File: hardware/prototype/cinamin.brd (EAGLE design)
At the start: 160 x 100 mm, 93 parts, among them J1 TC2030-JLINK-L, Q1 MOSFET-NCHANNELXFDN-3, Q2 MOSFET-NCHANNELXFDN-3, Q5 MOSFET-NCHANNELXFDN-3, U1 ADM8641, U11 ADM8641, U2 ADM8641, U3 BQ25504RGT

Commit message: most of the way through layout
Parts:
- removed JP21: TO_BQ25504, SparkFun-Passives:1X02
- removed JP23: FOR_BQ25504, SparkFun-Passives:1X02
- removed U$10, U$5: U1, chips:DFN-8
- removed U$11: M08X2, SparkFun-Connectors:2X8
- removed U$12: (no value), chips:TSOP-10
- removed U$13: (no value), fets:XFDFN-3
- removed U$6: (no value), chips:QFN-48-6MM
- removed U11: ADM8641, chips:WLCSP-6
- added PV_TO_CAPS: FOR_BQ25504, SparkFun-Passives:1X02
- added Q13: (no value), fets:XFDFN-3
- added R16: 2.2k, passives:0402_RES
- added RESET: B3U-1000P, switches:B3U-1000P
- added SOLAR_TO_BQ: TO_BQ25504, SparkFun-Passives:1X02
- added SUPPLY_SELECTOR: M08X2, SparkFun-Connectors:2X8
- added TP3, TP4, TP5, TP6, TP7, TP8: TPSPAD1-13, testpad:P1-13
- added U4, U5: U1, chips:DFN-8
- added U6: ADM8641, chips:WLCSP-6
- added U7: (no value), chips:TSOP-10
- added U9: (no value), chips:QFN-48-6MM
- JP22: value (none) -> TO_BLE
- JP24: value (none) -> TO_BQ25504
- TP1, TP2: value TPSQB1,27 -> TPSPAD1-13; device testpad:B1,27 -> testpad:P1-13
- moved JP24 453.2 mm to (20.0, 11.8), flipped to the bottom, turned to 180 degrees
- moved JP22 449.9 mm to (27.4, 11.8)
- moved C14 440.8 mm to (22.8, 9.30), turned to 180 degrees
- moved R22 432.9 mm to (19.1, 5.70), turned to 90 degrees
- moved R21 427.5 mm to (19.1, 3.90), turned to 90 degrees
- moved R20 426.1 mm to (21.0, 5.70), turned to 90 degrees
- moved R19 420.7 mm to (21.0, 3.90), turned to 90 degrees
- moved C13 417.2 mm to (27.8, 6.20), turned to 270 degrees
- moved R18 416.9 mm to (22.3, 3.50), turned to 180 degrees
- moved C12 414.2 mm to (26.8, 6.20), turned to 270 degrees
- moved C11 401.9 mm to (19.9, 8.20), turned to 270 degrees
- moved L3 399.3 mm to (21.2, 8.00), turned to 90 degrees
- moved JP20 391.2 mm to (42.6, 23.8)
- moved JP18 389.2 mm to (38.2, 37.5)
- moved JP19 382.2 mm to (35.4, 23.7)
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- renumbered U$8 to U8
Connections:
- removed net N$48: C14.2, R18.1, R21.1
- new net HIGH: JP20.1, Q10.D
- new net N$52: J1.2, U9.30
- new net N$53: J1.4, U9.31
- new net N$56: R16.2, RESET.1, U9.21
- new net OUT: JP2.1, R3.1, U4.P8
- new net OUT2: JP22.1, Q13.D
- new net VDD: JP19.2, Q10.S, U7.10
- new net VIN_DC: JP24.2, U3.2
- new net VSTOR: C12.1, C13.1, Q13.S, U3.15, U3.3
- net 580_VBAT: now also J1.1, RESET.2, U9.17, U9.19; no longer C12.1, C13.1, JP2.1, JP20.1, JP22.1, Q10.D, R3.1, U$13.D, U$13.S, U$5.P8, U$6.17, U$6.19, U3.15, U3.3
- net ADM8641: now also SUPPLY_SELECTOR.6; no longer U$11.6
- net ADM8641_2: now also SUPPLY_SELECTOR.12; no longer U$11.12
- net AP4400: now also SUPPLY_SELECTOR.10; no longer JP19.2, Q10.S, U$11.10, U$12.10
- net BQ25504: now also SUPPLY_SELECTOR.8; no longer U$11.8
- net GND: now also C14.2, J1.5, R16.1, R18.1, R21.1, TP6.TP, TP7.TP, TP8.TP, U4.P$1, U4.P1, U4.P2, U5.P$1, U5.P1, U5.P2, U6.A2, U6.B2, U7.5, U9.20, U9.28, U9.41, U9.GND; no longer U$10.P$1, U$10.P1, U$10.P2, U$12.5, U$5.P$1, U$5.P1, U$5.P2, U$6.20, U$6.28, U$6.41, U$6.GND, U11.A2, U11.B2
- net LTC1540_E_HYST: now also SUPPLY_SELECTOR.4; no longer U$11.4
- net LTC1540_I_HYST: now also SUPPLY_SELECTOR.2; no longer U$11.2
- net N$1: now also PV_TO_CAPS.2, SUPPLY_SELECTOR.1, SUPPLY_SELECTOR.11, SUPPLY_SELECTOR.3, SUPPLY_SELECTOR.5, SUPPLY_SELECTOR.7, SUPPLY_SELECTOR.9; no longer JP23.2, U$11.1, U$11.11, U$11.3, U$11.5, U$11.7, U$11.9
- net N$10: now also U9.34; no longer U$6.34
- net N$11: now also U9.35; no longer U$6.35
- net N$14: now also U5.P3; no longer U$10.P3
- net N$2: now also U5.P4, U5.P5, U5.P6; no longer U$10.P4, U$10.P5, U$10.P6
- net N$20: now also U5.P7; no longer U$10.P7
- net N$28: now also U4.P7; no longer U$5.P7
- net N$29: now also U6.C2; no longer U11.C2
- net N$3: now also U4.P3; no longer U$5.P3
- net N$35: now also U6.A1; no longer U11.A1
- net N$37: now also U7.6; no longer U$12.6
- net N$4: now also U4.P4, U4.P5, U4.P6; no longer U$5.P4, U$5.P5, U$5.P6
- net N$43: now also PV_TO_CAPS.1, SOLAR_TO_BQ.1, TP3.TP, TP4.TP, TP5.TP; no longer JP21.1, JP23.1
- net N$47: now also Q13.G; no longer U$13.G
- net N$5: now also U9.42; no longer U$6.42
- net N$7: now also U9.26; no longer U$6.26
- net N$8: now also U9.23, U9.37; no longer U$6.23, U$6.37
- net N$9: now also U5.P8; no longer U$10.P8
- net PV: now also SOLAR_TO_BQ.2; no longer JP21.2, JP24.2, U3.2
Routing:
- net N$43: track 0.00 -> 53.8 mm
- net N$1: track 0.00 -> 32.1 mm
- net 580_VBAT: track 0.00 -> 31.3 mm
- net N$52: track 0.00 -> 16.1 mm
- net N$8: track 0.00 -> 15.6 mm, vias 0 -> 2
- net GND: track 0.00 -> 15.0 mm, vias 0 -> 39
- net PV: track 0.00 -> 14.7 mm
- net ADM8641: track 0.00 -> 14.4 mm
- net VSTOR: track 0.00 -> 14.0 mm
- net N$19: track 0.00 -> 13.1 mm
- net N$41: track 0.00 -> 12.0 mm, vias 0 -> 2
- net N$53: track 0.00 -> 11.2 mm
- net LTC1540_E_HYST: track 0.00 -> 11.1 mm
- net N$47: track 0.00 -> 9.80 mm
- net N$25: track 0.00 -> 9.63 mm
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- added copper zone on layer 1, net GND
- added copper zone on layer 16, net GND
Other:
- board text added: "ADM8641_1"
- board text added: "ADM8641_2"
- board text added: "AP4400"
- board text added: "BQ25504"
- board text added: "Bluetooth"
- board text added: "Buffer Caps"
- board text added: "LTC1540_1"
- board text added: "LTC1540_2"
- board text added: "PV+"
- board text added: "PV-"
- board text removed: "Example BLE Layout"

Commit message: layout and schematic done
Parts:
- removed JP1, JP12, JP2, JP3: TO_BLE, SparkFun-Passives:1X02
- removed JP10, JP5: INPUT_DIVIDER, SparkFun-Passives:1X02
- removed JP11: TO_LTC1540, SparkFun-Passives:1X02
- removed JP13, JP6: STAGE_1_PULL, SparkFun-Passives:1X02
- removed JP14, JP7: STAGE_2_PULL, SparkFun-Passives:1X02
- removed JP15, JP9: OFF_DIVIDER, SparkFun-Passives:1X02
- removed JP16: TO_ADM, SparkFun-Passives:1X02
- removed JP17: TO_ADM2, SparkFun-Passives:1X02
- removed JP18: TO_ADM1, SparkFun-Passives:1X02
- removed JP19, JP20: TO_AP440, SparkFun-Passives:1X02
- removed JP4: (no value), SparkFun-Passives:1X02
- removed JP8: TO_LATCH, SparkFun-Passives:1X02
- removed U$7: AF212M, chips:AH212M
- added A1: (no value), chips:AH212M
- added J10, J15, J18, J3: TO_BLE, SparkFun-Passives:1X02
- added J11: TO_ADM, SparkFun-Passives:1X02
- added J12, J7: STAGE_1_PULL, SparkFun-Passives:1X02
- added J13, J8: STAGE_2_PULL, SparkFun-Passives:1X02
- added J14, J9: OFF_DIVIDER, SparkFun-Passives:1X02
- added J16: TO_ADM2, SparkFun-Passives:1X02
- added J17: TO_ADM1, SparkFun-Passives:1X02
- added J19, J20: TO_AP440, SparkFun-Passives:1X02
- added J2: TO_LTC1540, SparkFun-Passives:1X02
- added J4: INPUT_DIVIDER, SparkFun-Passives:1X02
- added J5: (no value), SparkFun-Passives:1X02
- added J6: TO_LATCH, SparkFun-Passives:1X02
- added PROG: TC2030-JLINK-L, connector:TC2030-IDC
- J1: value TC2030-JLINK-L -> INPUT_DIVIDER; device connector:TC2030-IDC -> SparkFun-Passives:1X02
- R1, R4: value (none) -> 2.2M
- R10, R11, R12, R13, R14, R15, R6, R7, R8, R9: value (none) -> 1M
- R2, R5: value (none) -> 1.18M
- R3: value (none) -> 3M
- U$9: device chips:AH212M -> chips:AH212M@1
- U1: value ADM8641 -> 3.048
- U2: value ADM8641 -> 2.3
- moved X1 92.4 mm to (68.6, 5.61), turned to 90 degrees
- moved C7 92.3 mm to (73.4, 4.46), turned to 180 degrees
- moved U9 84.0 mm to (74.0, 8.50), turned to 180 degrees
- moved L1 83.1 mm to (69.4, 10.3), turned to 180 degrees
- moved C5 80.3 mm to (69.0, 12.1), turned to 90 degrees
- moved C2 79.8 mm to (69.8, 12.1), turned to 90 degrees
- moved J1 79.0 mm to (49.8, 36.6)
- moved R16 74.3 mm to (72.9, 13.8), turned to 180 degrees
- moved RESET 70.8 mm to (72.9, 15.6), turned to 0 degrees
- moved R8 57.4 mm to (59.5, 18.9)
- moved R9 57.4 mm to (59.5, 17.1)
- moved Q4 57.3 mm to (58.0, 26.0)
- moved R4 57.3 mm to (45.7, 21.0)
- moved R5 57.3 mm to (45.7, 19.3)
- moved R6 57.3 mm to (53.7, 18.8)
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- renumbered JP22 to J22, JP24 to J21, U$1 to D4, U$2 to D3, U$3 to D2, U$4 to D1
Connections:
- removed net N$13: C10.P$1, C9.P$1, L2.2, U8.A2, U8.F2
- new net N$48: X2.1
- new net N$55: U8.F2
- new net N$57: C10.P$1
- new net N$58: C9.P$1
- net 580_VBAT: now also J10.2, J15.2, J18.2, J20.2, J3.2, PROG.1; no longer J1.1, JP1.2, JP12.2, JP2.2, JP20.2, JP3.2
- net ADM8641: now also J11.2, J12.2, J13.2; no longer JP13.2, JP14.2, JP16.2
- net ADM8641_2: now also J16.2, J17.1, SUPPLY_SELECTOR.8; no longer JP17.2, JP18.1, SUPPLY_SELECTOR.12
- net AP4400: now also J19.1; no longer JP19.1
- net BQ25504: now also SUPPLY_SELECTOR.12; no longer SUPPLY_SELECTOR.8
- net GND: now also PROG.5; no longer C10.P$2, C8.P$2, C9.P$2, J1.5, U8.A3, U8.A5, U8.B4, U8.C3, U8.D3, U8.D4, U8.E1, U8.F3, X2.2, X2.4
- net HIGH: now also J20.1; no longer JP20.1
- net LTC1540_E_HYST: now also J4.2, J5.2, J6.1; no longer JP4.2, JP5.2, JP8.1
- net LTC1540_I_HYST: now also J1.2, J2.1; no longer JP10.2, JP11.1
- net N$12: no longer U8.F1
- net N$16: no longer U8.B1
- net N$17: no longer X2.1
- net N$18: now also J4.1; no longer JP5.1
- net N$20: now also J5.1; no longer JP4.1
- net N$21: now also J7.1; no longer JP6.1
- net N$22: now also J8.1; no longer JP7.1
- net N$24: now also J10.1, J9.2; no longer JP3.1, JP9.2
- net N$25: now also J6.2, J7.2, J8.2; no longer JP6.2, JP7.2, JP8.2
- net N$26: now also J9.1; no longer JP9.1
- net N$27: now also J1.1; no longer JP10.1
- net N$28: now also J2.2; no longer JP11.2
- net N$32: now also J14.2, J15.1; no longer JP12.1, JP15.2
- net N$33: now also J12.1; no longer JP13.1
- net N$34: now also J13.1; no longer JP14.1
- net N$35: now also J11.1; no longer JP16.1
- net N$36: now also J14.1; no longer JP15.1
- net N$38: now also J18.1; no longer JP1.1
- net N$40: now also J16.1; no longer JP17.1
- net N$42: now also J17.2; no longer JP18.2
- net N$5: now also A1.P1; no longer U$7.P1
- net N$52: now also PROG.2; no longer J1.2
- net N$53: now also PROG.4; no longer J1.4
- net N$6: now also U8.A2; no longer C8.P$1, U$9.P1, U8.A4
- net OUT: now also J3.1; no longer JP2.1
- net VDD: now also J19.2; no longer JP19.2
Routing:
- net 580_VBAT: track 31.3 -> 124.3 mm
- net ADM8641: track 14.4 -> 71.5 mm
- net LTC1540_E_HYST: track 11.1 -> 51.0 mm
- net LTC1540_I_HYST: track 3.68 -> 39.5 mm
- net BQ25504: track 6.57 -> 31.2 mm
- net AP4400: track 0.00 -> 16.9 mm
- net ADM8641_2: track 2.87 -> 18.3 mm
- net N$5: track 2.31 -> 3.80 mm
- net OUT2: track 7.53 -> 8.22 mm
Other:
- board size 160 x 100 mm -> 78.1 x 45.9 mm

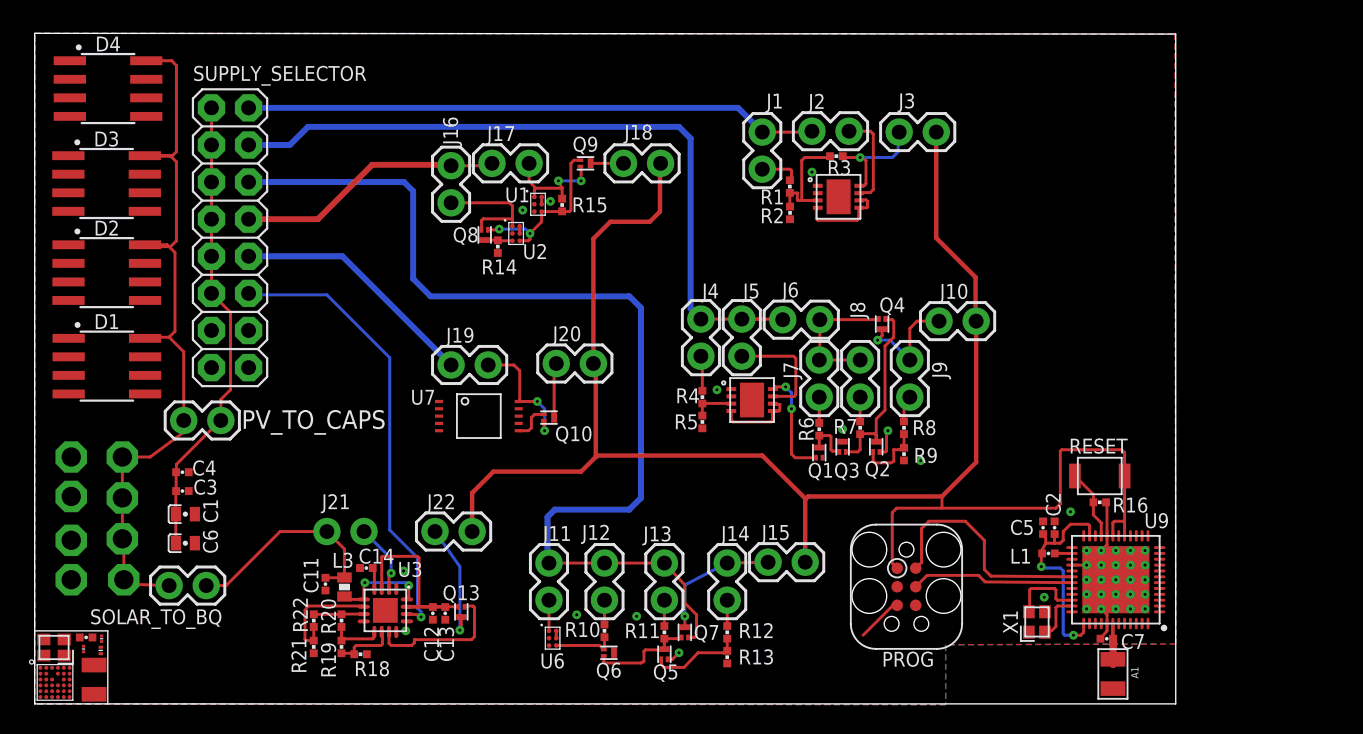
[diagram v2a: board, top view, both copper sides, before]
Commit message: added series parrallel solar jumps
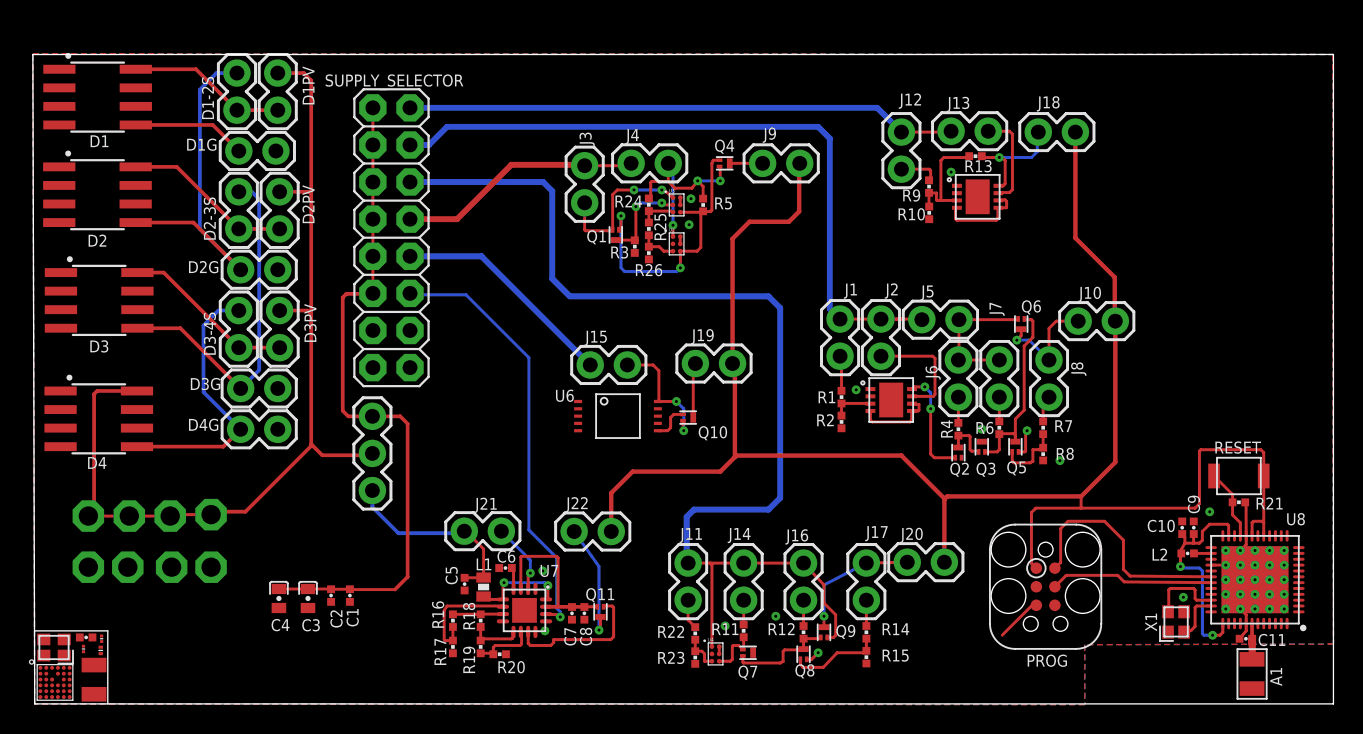
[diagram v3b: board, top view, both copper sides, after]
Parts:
- removed PV_TO_CAPS: FOR_BQ25504, SparkFun-Passives:1X02
- removed Q13: (no value), fets:XFDFN-3
- removed SOLAR_TO_BQ: TO_BQ25504, SparkFun-Passives:1X02
- added D1-2S, D2-3S, D3-4S: SER, SparkFun-Passives:1X02
- added D1G, D2G, D3G, D4G: GND, SparkFun-Passives:1X02
- added D1PV, D2PV, D3PV: HIGH, SparkFun-Passives:1X02
- added PV_TO_CAP: (no value), SparkFun-Connectors:1X03
- added Q11: (no value), fets:XFDFN-3
- added R17: 5.23M, passives:0402_RES
- added R23: 1.43M, passives:0402_RES
- added R24: 2.87M, passives:0402_RES
- added R25: 715k, passives:0402_RES
- added R26: 1.47M, passives:0402_RES
- A1: value (none) -> AH212M
- A2: value AF212M -> AH212M
- C1: value 100uF -> 15uF; device passives:CAP0603 -> passives:0402_CAP
- C10: value 1uF -> 100nF; device passives:01005_CAP -> passives:0402_CAP
- C11: value 4.7uF -> 1pF
- C12: value 0.1uF -> 1uF; device passives:0402_CAP -> passives:01005_CAP
- C13: value 4.7uF -> 100nF; device passives:0402_CAP -> passives:01005_CAP
- C14: value .01uF -> 1pF; device passives:0402_CAP -> passives:0201_CAP
- C2: value 1uF -> 15uF
- C3, C4: value 15uF -> 100uF; device passives:0402_CAP -> passives:CAP0603
- C5: value 100nF -> 4.7uF
- C6: value 100uF -> .01uF; device passives:CAP0603 -> passives:0402_CAP
- C7: value 1pF -> 0.1uF
- C8: value 1pF -> 4.7uF; device passives:0201_CAP -> passives:0402_CAP
- C9: value 100nF -> 1uF; device passives:01005_CAP -> passives:0402_CAP
- D1, D2, D3, D4: value (none) -> CPC1822
- J12: value STAGE_1_PULL -> INPUT_DIVIDER
- J13: value STAGE_2_PULL -> TO_LTC1540
- J14: value OFF_DIVIDER -> STAGE_1_PULL
- J15: value TO_BLE -> TO_AP440
- J16: value TO_ADM2 -> STAGE_2_PULL
- J17: value TO_ADM1 -> OFF_DIVIDER
- J2: value TO_LTC1540 -> (none)
- J20: value TO_AP440 -> TO_BLE
- J3: value TO_BLE -> TO_ADM2
- J4: value INPUT_DIVIDER -> TO_ADM1
- J5: value (none) -> TO_LATCH
- J6: value TO_LATCH -> STAGE_1_PULL
- J7: value STAGE_1_PULL -> STAGE_2_PULL
- J8: value STAGE_2_PULL -> OFF_DIVIDER
- J9: value OFF_DIVIDER -> TO_BLE
- L1: value 2.2uH -> 22uH; device passives:0402_CAP -> passives:0603_CAP
- L2: value (none) -> 2.2uH
- L3: value 22uH -> 2.2uH; device passives:0603_CAP -> passives:0402_CAP
- Q1: value MOSFET-NCHANNELXFDN-3 -> (none)
- Q8: value (none) -> MOSFET-NCHANNELXFDN-3
- R10: value 1M -> 1.18M
- R13: value 1M -> 3M
- R16: value 2.2k -> 4.87M
- R18: value 3.67M -> 3.24M
- R19: value 3.088M -> 3.09M
- R20: value 3.23M -> 3.65M
- R21: value 5.2M -> 2.2k
- R22: value 4.8M -> 3.48M
- R3: value 3M -> 1M
- R4: value 2.2M -> 1M
- R5: value 1.18M -> 1M
- R9: value 1M -> 2.2M
- U1: value 3.048 -> LTC1540; device chips:WLCSP-6 -> chips:DFN-8
- U2: value 2.3 -> (none)
- U3: value BQ25504RGT -> (none); device chips:S-PVQFN-N16 -> chips:WLCSP-6
- U4: value U1 -> (none); device chips:DFN-8 -> chips:WLCSP-6
- U5: value U1 -> ltc1540
- U6: value ADM8641 -> AP4400_3.4_2.3; device chips:WLCSP-6 -> chips:TSOP-10
- U7: value (none) -> BQ25504RGT; device chips:TSOP-10 -> chips:S-PVQFN-N16
- U8: value (none) -> DA14580; device chips:WLCSP34 -> chips:QFN-48-6MM
- U9: device chips:QFN-48-6MM -> chips:WLCSP34
- X1, X2: value (none) -> 16Mhz
- moved U8 83.5 mm to (83.5, 8.50), turned to 180 degrees
- moved C10 75.7 mm to (78.5, 12.1), turned to 90 degrees
- moved L2 75.6 mm to (78.9, 10.3)
- moved C9 75.1 mm to (79.3, 12.1), turned to 90 degrees
- moved U9 74.0 mm to (0.39, 0.47), turned to 0 degrees
- moved R21 64.1 mm to (82.4, 13.8), turned to 180 degrees
- moved C11 63.1 mm to (82.9, 4.46), turned to 180 degrees
- moved C2 49.7 mm to (20.3, 7.42), turned to 270 degrees
- moved R16 45.0 mm to (28.6, 5.70), turned to 90 degrees
- moved C5 39.8 mm to (29.4, 8.20), turned to 270 degrees
- moved J17 39.4 mm to (56.9, 7.10), turned to 90 degrees
- moved L1 38.7 mm to (30.7, 8.00), turned to 90 degrees
- moved R13 38.3 mm to (64.4, 37.5), turned to 180 degrees
- moved J13 37.6 mm to (62.7, 39.2), turned to 0 degrees
- moved R15 37.3 mm to (56.9, 3.20)
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- renumbered U$9 to A2
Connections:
- removed net N$18 (its old number): J4.1, R4.2
- removed net N$26 (its old number): J9.1, R8.2
- removed net N$4 (its old number): U4.P4, U4.P5, U4.P6
- new net N$13: J11.1, R22.2
- new net N$2: U1.P4, U1.P5, U1.P6
- new net N$21: J6.1, R4.2
- new net N$27: J12.1, R9.2
- new net N$59: R22.1, R23.2, U4.C1
- new net N$60: R25.1, R26.2, U2.C1
- new net N$61: D1.5, D1G.2
- new net N$62: D1-2S.2, D2.5, D2G.2
- new net N$63: D2-3S.2, D3.5, D3G.2
- new net N$65: D1-2S.1, D1.8, D1PV.2
- new net N$66: D1PV.1, D2PV.1, D3PV.1, D4.8, PV_TO_CAP.2, TP1.TP, TP3.TP, TP4.TP, TP5.TP
- new net N$67: D2-3S.1, D2.8, D2PV.2
- new net N$68: D3-4S.1, D3.8, D3PV.2
- net 580_VBAT: now also J19.2, J9.2, U8.17, U8.19; no longer J15.2, J3.2, U9.17, U9.19
- net ADM8641: now also J14.2, J16.2, Q9.S, U4.A1; no longer J12.2, J13.2, Q7.S
- net ADM8641_2: now also J3.2, J4.1; no longer J16.2, J17.1
- net AP4400: now also J15.1; no longer J19.1
- net BQ25504: now also U7.14; no longer U3.14
- net GND: now also C1.2, C10.2, C3.NEG, C4.NEG, C6.2, C8.2, C9.2, D1G.1, D2G.1, D3G.1, D4G.1, Q7.D, Q8.S, R10.1, R15.1, R17.1, R20.1, R23.1, R26.1, R3.1, R8.1, U1.P$1, U1.P1, U1.P2, U3.A2, U3.B2, U4.A2, U4.B2, U6.5, U7.1, U7.12, U7.13, U8.20, U8.28, U8.41, U8.GND; no longer C1.NEG, C12.2, C13.2, C14.2, C3.2, C4.2, C6.NEG, D1.5, D2.5, D3.5, D4.5, Q1.S, Q6.D, R13.1, R14.1, R16.1, R18.1, R5.1, R9.1, U1.A2, U1.B2, U3.1, U3.12, U3.13, U4.P$1, U4.P1, U4.P2, U6.A2, U6.B2, U7.5, U9.20, U9.28, U9.41, U9.GND
- net HIGH: now also J19.1; no longer J20.1
- net LTC1540_E_HYST: now also J1.2, J2.2, J5.1; no longer J4.2, J5.2, J6.1
- net LTC1540_I_HYST: now also J12.2, J13.1; no longer J1.2, J2.1
- net N$1: now also C1.1, C2.1, C3.POS, C4.POS, PV_TO_CAP.3; no longer C1.POS, C3.1, C4.1, C6.POS, PV_TO_CAPS.2
- net N$10: now also U8.34; no longer U9.34
- net N$11: now also U8.35; no longer U9.35
- net N$12: now also L3.1; no longer L2.1
- net N$14: now also R1.1, R2.2, U1.P3; no longer R4.1, R5.2, U5.P3
- net N$15: now also Q2.D, R4.1; no longer Q1.D, R6.1
- net N$17: now also U9.A1; no longer U8.A1
- net N$19: now also Q5.D, Q6.G, R6.1; no longer Q2.D, Q4.G, R7.1
- net N$20: now also J2.1, U1.P7; no longer J5.1, U5.P7
- net N$23: now also Q5.G, R7.1, R8.2; no longer Q2.G, R8.1, R9.2
- net N$24: now also J8.2, Q6.D; no longer J9.2, Q4.D
- net N$25: now also J5.2, Q6.S; no longer J8.2, Q4.S
- net N$28: now also J13.2, U5.P7; no longer J2.2, U4.P7
- net N$29: now also Q7.G, R11.1, U4.C2; no longer Q6.G, R10.1, U6.C2
- net N$3: now also R10.2, R13.2, R9.1, U5.P3; no longer R1.1, R2.2, R3.2, U4.P3
- net N$30: now also Q7.S, Q8.D, Q9.G, R12.1; no longer Q5.D, Q6.S, Q7.G, R11.1
- net N$31: now also Q8.G, R14.1, R15.2; no longer Q5.G, R12.1, R13.2
- net N$32: now also J17.2, J20.1, Q9.D; no longer J14.2, J15.1, Q7.D
- net N$33: now also J14.1, R11.2; no longer J12.1, R10.2
- net N$34: now also J16.1, R12.2; no longer J13.1, R11.2
- net N$35: now also R24.1, R25.2, U3.C1; no longer J11.1, U6.A1
- net N$36: now also J17.1, R14.2; no longer J14.1, R12.2
- net N$37: now also U6.6; no longer U7.6
- net N$38: now also J9.1, Q4.D; no longer J18.1, Q9.D
- net N$39: now also Q1.D, R3.2, U3.B1; no longer Q8.D, R14.2, U2.C1
- net N$40: now also J3.1, Q1.S, U3.A1; no longer J16.1, Q8.S, U2.A1
- net N$41: now also Q1.G, Q4.G, R5.1, U3.C2; no longer Q8.G, Q9.G, R15.1, U1.C2
- net N$42: now also J4.2, Q4.S, R24.2, R5.2, U2.A1; no longer J17.2, Q9.S, R15.2, U1.A1
- net N$43: now also D3-4S.2, D4.5, D4G.2; no longer D1.8, D2.8, D3.8, D4.8, PV_TO_CAPS.1, SOLAR_TO_BQ.1, TP1.TP, TP3.TP, TP4.TP, TP5.TP
- net N$44: now also L1.1, U7.16, U7.5; no longer L3.1, U3.16, U3.5
- net N$45: now also U7.8; no longer U3.8
- net N$46: now also R16.2, R18.2, U7.7; no longer R20.2, R22.2, U3.7
- net N$47: now also Q11.G, U7.11; no longer Q13.G, U3.11
- net N$49: now also R18.1, U7.9; no longer R20.1, U3.9
- net N$5: now also C11.1, U8.42; no longer C7.1, U9.42
- net N$50: now also R20.2, U7.10; no longer R18.2, U3.10
- net N$51: now also C6.1, U7.4; no longer C14.1, U3.4
- net N$52: now also U8.30; no longer U9.30
- net N$53: now also U8.31; no longer U9.31
- net N$54: now also R16.1, R17.2, U7.6; no longer R21.2, R22.1, U3.6
- net N$55: now also U9.F2; no longer U8.F2
- net N$56: now also R21.2, U8.21; no longer R16.2, U9.21
- net N$57: now also C12.P$1; no longer C10.P$1
- net N$58: now also C13.P$1; no longer C9.P$1
- net N$6: now also U9.A2; no longer U8.A2
- net N$7: now also L2.1, U8.26; no longer L1.1, U9.26
- net N$8: now also C10.1, C9.1, L2.2, U8.23, U8.37; no longer C2.1, C5.1, L1.2, U9.23, U9.37
- net N$9: now also Q2.G, U1.P8; no longer Q1.G, U5.P8
- net OUT: now also J18.1, R13.1, U5.P8; no longer J3.1, R3.1, U4.P8
- net OUT2: now also Q11.D; no longer Q13.D
- net PV: now also C5.1, L1.2, PV_TO_CAP.1; no longer C11.1, L3.2, SOLAR_TO_BQ.2
- net VDD: now also J15.2, U6.10; no longer J19.2, U7.10
- net VIN_DC: now also U7.2; no longer U3.2
- net VSTOR: now also C7.1, C8.1, Q11.S, U7.15, U7.3; no longer C12.1, C13.1, Q13.S, U3.15, U3.3
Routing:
- net N$66: track 0.00 -> 65.2 mm
- net N$43: track 53.8 -> 18.6 mm
- net N$62: track 0.00 -> 25.0 mm
- net N$63: track 0.00 -> 23.9 mm
- net N$1: track 32.1 -> 47.2 mm
- net N$68: track 0.00 -> 11.9 mm
- net N$67: track 0.00 -> 11.6 mm
- net N$65: track 0.00 -> 10.9 mm
- net N$41: track 12.0 -> 20.5 mm
- net N$61: track 0.00 -> 7.79 mm
- net N$42: track 8.16 -> 15.1 mm, vias 2 -> 3
- net N$4 (its old number): track 6.16 -> 0.00 mm
- net N$2: track 0.00 -> 5.60 mm
- net N$39: track 1.92 -> 6.79 mm, vias 0 -> 2
- net ADM8641: track 71.5 -> 75.7 mm
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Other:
- board size 78.1 x 45.9 mm -> 89 x 44.5 mm
- board text added: "BQ"
- board text added: "CAP"
- board text added: "Cinamin Beacon Evaluation Board Rev_A Joshua Adkins 08/2015"

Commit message: committing board sent to fab
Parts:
- moved TP3 28.3 mm to (10.4, 40.9)
- moved TP6 28.2 mm to (10.4, 37.3)
- moved TP2 22.3 mm to (10.4, 30.6)
- moved TP4 21.6 mm to (10.4, 34.4)
- moved TP1 15.7 mm to (10.4, 27.1)
- moved TP7 14.0 mm to (10.4, 23.4)
- moved TP5 6.19 mm to (10.4, 18.9)
- moved TP8 6.11 mm to (10.4, 15.2)
- moved D1-2S 2.50 mm to (14.5, 38.2)
- moved D3PV 2.50 mm to (17.4, 24.5)
- moved D2-3S 2.50 mm to (14.6, 30.1)
- moved D3 2.50 mm to (5.05, 25.2)
- moved D3-4S 2.50 mm to (14.6, 22.0)
- moved D4 2.50 mm to (5.02, 17.1)
- moved D2G 2.50 mm to (17.3, 27.3)
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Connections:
- net GND: no longer TP2.TP, TP6.TP, TP7.TP, TP8.TP
- net N$43: now also TP8.TP
- net N$61: now also TP6.TP
- net N$62: now also TP2.TP
- net N$63: now also TP7.TP
- net N$65: now also TP3.TP
- net N$66: no longer TP1.TP, TP3.TP, TP4.TP
- net N$67: now also TP4.TP
- net N$68: now also TP1.TP
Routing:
- net N$66: track 65.2 -> 46.1 mm
- net GND: track 14.6 -> 12.4 mm, vias 39 -> 40
- net N$68: track 11.9 -> 12.4 mm
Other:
- board text removed: "PV+"
- board text removed: "PV-"
